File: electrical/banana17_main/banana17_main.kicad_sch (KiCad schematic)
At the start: 25 parts, among them J1 78171-0004, U1 RP2040, U2 NCP1117-3.3_SOT223, U3 W25Q128JVS, Y1 ABMB-272-T3

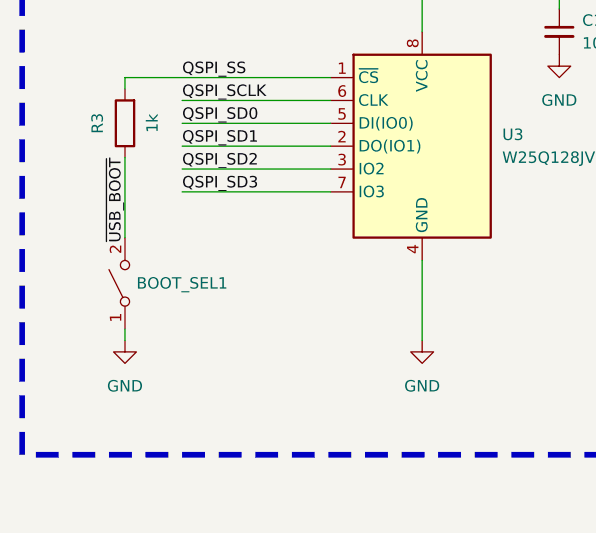
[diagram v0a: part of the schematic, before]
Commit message: Reverted change for SSD1306 library import.
Reverted change for SSD1306 library import.
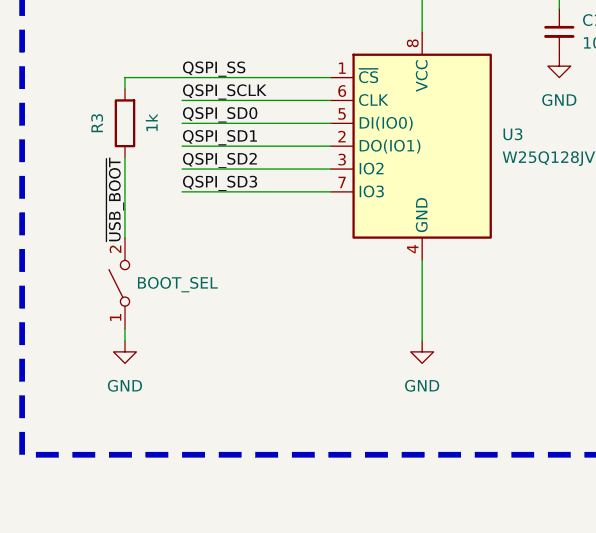
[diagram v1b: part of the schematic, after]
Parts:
- renumbered BOOT_SEL1 to BOOT_SEL
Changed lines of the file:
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@@
 		(on_board yes)
 		(dnp no)
-		(property "Reference" "#PWR019"
+		(property "Reference" "#PWR017"
 			(at 115.57 167.64 0)
 			(effects
@@
 			(project "banana17_main"
 				(path "/fd2b462c-d7c2-4bbf-9a41-8b3fef737a65"
-					(reference "#PWR019")
+					(reference "#PWR017")
 					(unit 1)
 				)
@@
 		(on_board yes)
 		(dnp no)
-		(property "Reference" "#PWR017"
+		(property "Reference" "#PWR019"
 			(at 129.54 160.02 0)
 			(effects
@@
 			(project "banana17_main"
 				(path "/fd2b462c-d7c2-4bbf-9a41-8b3fef737a65"
-					(reference "#PWR017")
+					(reference "#PWR019")
 					(unit 1)
 				)
@@
 		(dnp no)
 		(fields_autoplaced yes)
-		(property "Reference" "#PWR01"
+		(property "Reference" "#PWR03"
 			(at 219.71 39.37 0)
 			(effects
@@
 			(project "banana17_main"
 				(path "/fd2b462c-d7c2-4bbf-9a41-8b3fef737a65"
-					(reference "#PWR01")
+					(reference "#PWR03")
 					(unit 1)
 				)
@@
 		(on_board yes)
 		(dnp no)
-		(property "Reference" "#PWR013"
+		(property "Reference" "#PWR020"
 			(at 137.16 107.95 0)
 			(effects
@@
 			(project "banana17_main"
 				(path "/fd2b462c-d7c2-4bbf-9a41-8b3fef737a65"
-					(reference "#PWR013")
+					(reference "#PWR020")
 					(unit 1)
 				)
@@
 		(on_board yes)
 		(dnp no)
-		(property "Reference" "#PWR07"
+		(property "Reference" "#PWR021"
 			(at 151.13 90.17 0)
 			(effects
@@
 			(project "banana17_main"
 				(path "/fd2b462c-d7c2-4bbf-9a41-8b3fef737a65"
-					(reference "#PWR07")
+					(reference "#PWR021")
 					(unit 1)
 				)
@@
 		(dnp no)
 		(fields_autoplaced yes)
-		(property "Reference" "#PWR010"
+		(property "Reference" "#PWR08"
 			(at 43.18 107.95 0)
 			(effects
@@
 			(project "banana17_main"
 				(path "/fd2b462c-d7c2-4bbf-9a41-8b3fef737a65"
-					(reference "#PWR010")
+					(reference "#PWR08")
 					(unit 1)
 				)
@@
 		(dnp no)
 		(fields_autoplaced yes)
-		(property "Reference" "BOOT_SEL1"
+		(property "Reference" "BOOT_SEL"
 			(at 36.83 168.9099 90)
 			(effects
@@
 			(project "banana17_main"
 				(path "/fd2b462c-d7c2-4bbf-9a41-8b3fef737a65"
-					(reference "BOOT_SEL1")
+					(reference "BOOT_SEL")
 					(unit 1)
 				)
@@
 		(on_board yes)
 		(dnp no)
-		(property "Reference" "#PWR020"
+		(property "Reference" "#PWR016"
 			(at 35.56 181.61 0)
 			(effects
@@
 			(project "banana17_main"
 				(path "/fd2b462c-d7c2-4bbf-9a41-8b3fef737a65"
-					(reference "#PWR020")
+					(reference "#PWR016")
 					(unit 1)
 				)
@@
 		(dnp no)
 		(fields_autoplaced yes)
-		(property "Reference" "#PWR012"
+		(property "Reference" "#PWR010"
 			(at 83.82 107.95 0)
 			(effects
@@
 			(project "banana17_main"
 				(path "/fd2b462c-d7c2-4bbf-9a41-8b3fef737a65"
-					(reference "#PWR012")
+					(reference "#PWR010")
 					(unit 1)
 				)
@@
 		(dnp no)
 		(fields_autoplaced yes)
-		(property "Reference" "#PWR08"
+		(property "Reference" "#PWR011"
 			(at 30.48 93.98 0)
 			(effects
@@
 			(project "banana17_main"
 				(path "/fd2b462c-d7c2-4bbf-9a41-8b3fef737a65"
-					(reference "#PWR08")
+					(reference "#PWR011")
 					(unit 1)
 				)
@@
 		(dnp no)
 		(fields_autoplaced yes)
-		(property "Reference" "#PWR011"
+		(property "Reference" "#PWR09"
 			(at 63.5 107.95 0)
 			(effects
@@
 			(project "banana17_main"
 				(path "/fd2b462c-d7c2-4bbf-9a41-8b3fef737a65"
-					(reference "#PWR011")
+					(reference "#PWR09")
 					(unit 1)
 				)
@@
 		(dnp no)
 		(fields_autoplaced yes)
-		(property "Reference" "#PWR04"
+		(property "Reference" "#PWR06"
 			(at 110.49 40.64 0)
 			(effects
@@
 			(project "banana17_main"
 				(path "/fd2b462c-d7c2-4bbf-9a41-8b3fef737a65"
-					(reference "#PWR04")
+					(reference "#PWR06")
 					(unit 1)
 				)
@@
 		(dnp no)
 		(fields_autoplaced yes)
-		(property "Reference" "#PWR09"
+		(property "Reference" "#PWR012"
 			(at 99.06 93.98 0)
 			(effects
@@
 			(project "banana17_main"
 				(path "/fd2b462c-d7c2-4bbf-9a41-8b3fef737a65"
-					(reference "#PWR09")
+					(reference "#PWR012")
 					(unit 1)
 				)
@@
 		(dnp no)
 		(fields_autoplaced yes)
-		(property "Reference" "#PWR06"
+		(property "Reference" "#PWR07"
 			(at 110.49 55.88 0)
 			(effects
@@
 			(project "banana17_main"
 				(path "/fd2b462c-d7c2-4bbf-9a41-8b3fef737a65"
-					(reference "#PWR06")
+					(reference "#PWR07")
 					(unit 1)
 				)
@@
 		(dnp no)
 		(fields_autoplaced yes)
-		(property "Reference" "#PWR03"
+		(property "Reference" "#PWR04"
 			(at 45.72 40.64 0)
 			(effects
@@
 			(project "banana17_main"
 				(path "/fd2b462c-d7c2-4bbf-9a41-8b3fef737a65"
-					(reference "#PWR03")
+					(reference "#PWR04")
 					(unit 1)
 				)
@@
 		(dnp no)
 		(fields_autoplaced yes)
-		(property "Reference" "#PWR016"
+		(property "Reference" "#PWR014"
 			(at 83.82 149.86 0)
 			(effects
@@
 			(project "banana17_main"
 				(path "/fd2b462c-d7c2-4bbf-9a41-8b3fef737a65"
-					(reference "#PWR016")
+					(reference "#PWR014")
 					(unit 1)
 				)
@@
 		(dnp no)
 		(fields_autoplaced yes)
-		(property "Reference" "#PWR014"
+		(property "Reference" "#PWR015"
 			(at 68.58 137.16 0)
 			(effects
@@
 			(project "banana17_main"
 				(path "/fd2b462c-d7c2-4bbf-9a41-8b3fef737a65"
-					(reference "#PWR014")
+					(reference "#PWR015")
 					(unit 1)
 				)
@@
 		(dnp no)
 		(fields_autoplaced yes)
-		(property "Reference" "#PWR015"
+		(property "Reference" "#PWR01"
 			(at 223.52 142.24 0)
 			(effects
@@
 			(project "banana17_main"
 				(path "/fd2b462c-d7c2-4bbf-9a41-8b3fef737a65"
-					(reference "#PWR015")
+					(reference "#PWR01")
 					(unit 1)
 				)
@@
 		(dnp no)
 		(fields_autoplaced yes)
-		(property "Reference" "#PWR021"
+		(property "Reference" "#PWR013"
 			(at 68.58 181.61 0)
 			(effects
@@
 			(project "banana17_main"
 				(path "/fd2b462c-d7c2-4bbf-9a41-8b3fef737a65"
-					(reference "#PWR021")
-					(unit 1)
-				)
+					(reference "#PWR013")
+					(unit 1)
+				)

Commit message: Uploaded library for SSD1306 128x32.
Uploaded library for SSD1306 128x32. This needs to be tested first prior to usage.
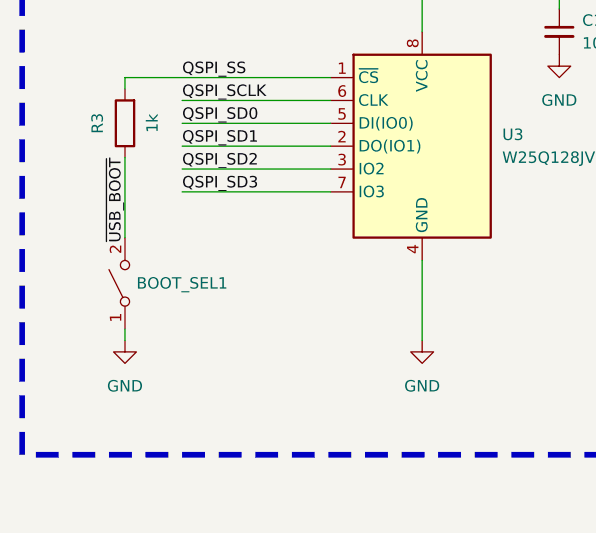
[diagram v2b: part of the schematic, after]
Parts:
- renumbered BOOT_SEL to BOOT_SEL1
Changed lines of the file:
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@@
 		(on_board yes)
 		(dnp no)
-		(property "Reference" "#PWR017"
+		(property "Reference" "#PWR019"
 			(at 115.57 167.64 0)
 			(effects
@@
 			(project "banana17_main"
 				(path "/fd2b462c-d7c2-4bbf-9a41-8b3fef737a65"
-					(reference "#PWR017")
+					(reference "#PWR019")
 					(unit 1)
 				)
@@
 		(on_board yes)
 		(dnp no)
-		(property "Reference" "#PWR019"
+		(property "Reference" "#PWR017"
 			(at 129.54 160.02 0)
 			(effects
@@
 			(project "banana17_main"
 				(path "/fd2b462c-d7c2-4bbf-9a41-8b3fef737a65"
-					(reference "#PWR019")
+					(reference "#PWR017")
 					(unit 1)
 				)
@@
 		(dnp no)
 		(fields_autoplaced yes)
-		(property "Reference" "#PWR03"
+		(property "Reference" "#PWR01"
 			(at 219.71 39.37 0)
 			(effects
@@
 			(project "banana17_main"
 				(path "/fd2b462c-d7c2-4bbf-9a41-8b3fef737a65"
-					(reference "#PWR03")
+					(reference "#PWR01")
 					(unit 1)
 				)
@@
 		(on_board yes)
 		(dnp no)
-		(property "Reference" "#PWR020"
+		(property "Reference" "#PWR013"
 			(at 137.16 107.95 0)
 			(effects
@@
 			(project "banana17_main"
 				(path "/fd2b462c-d7c2-4bbf-9a41-8b3fef737a65"
-					(reference "#PWR020")
+					(reference "#PWR013")
 					(unit 1)
 				)
@@
 		(on_board yes)
 		(dnp no)
-		(property "Reference" "#PWR021"
+		(property "Reference" "#PWR07"
 			(at 151.13 90.17 0)
 			(effects
@@
 			(project "banana17_main"
 				(path "/fd2b462c-d7c2-4bbf-9a41-8b3fef737a65"
-					(reference "#PWR021")
+					(reference "#PWR07")
 					(unit 1)
 				)
@@
 		(dnp no)
 		(fields_autoplaced yes)
-		(property "Reference" "#PWR08"
+		(property "Reference" "#PWR010"
 			(at 43.18 107.95 0)
 			(effects
@@
 			(project "banana17_main"
 				(path "/fd2b462c-d7c2-4bbf-9a41-8b3fef737a65"
-					(reference "#PWR08")
+					(reference "#PWR010")
 					(unit 1)
 				)
@@
 		(dnp no)
 		(fields_autoplaced yes)
-		(property "Reference" "BOOT_SEL"
+		(property "Reference" "BOOT_SEL1"
 			(at 36.83 168.9099 90)
 			(effects
@@
 			(project "banana17_main"
 				(path "/fd2b462c-d7c2-4bbf-9a41-8b3fef737a65"
-					(reference "BOOT_SEL")
+					(reference "BOOT_SEL1")
 					(unit 1)
 				)
@@
 		(on_board yes)
 		(dnp no)
-		(property "Reference" "#PWR016"
+		(property "Reference" "#PWR020"
 			(at 35.56 181.61 0)
 			(effects
@@
 			(project "banana17_main"
 				(path "/fd2b462c-d7c2-4bbf-9a41-8b3fef737a65"
-					(reference "#PWR016")
+					(reference "#PWR020")
 					(unit 1)
 				)
@@
 		(dnp no)
 		(fields_autoplaced yes)
-		(property "Reference" "#PWR010"
+		(property "Reference" "#PWR012"
 			(at 83.82 107.95 0)
 			(effects
@@
 			(project "banana17_main"
 				(path "/fd2b462c-d7c2-4bbf-9a41-8b3fef737a65"
-					(reference "#PWR010")
+					(reference "#PWR012")
 					(unit 1)
 				)
@@
 		(dnp no)
 		(fields_autoplaced yes)
-		(property "Reference" "#PWR011"
+		(property "Reference" "#PWR08"
 			(at 30.48 93.98 0)
 			(effects
@@
 			(project "banana17_main"
 				(path "/fd2b462c-d7c2-4bbf-9a41-8b3fef737a65"
-					(reference "#PWR011")
+					(reference "#PWR08")
 					(unit 1)
 				)
@@
 		(dnp no)
 		(fields_autoplaced yes)
-		(property "Reference" "#PWR09"
+		(property "Reference" "#PWR011"
 			(at 63.5 107.95 0)
 			(effects
@@
 			(project "banana17_main"
 				(path "/fd2b462c-d7c2-4bbf-9a41-8b3fef737a65"
-					(reference "#PWR09")
+					(reference "#PWR011")
 					(unit 1)
 				)
@@
 		(dnp no)
 		(fields_autoplaced yes)
-		(property "Reference" "#PWR06"
+		(property "Reference" "#PWR04"
 			(at 110.49 40.64 0)
 			(effects
@@
 			(project "banana17_main"
 				(path "/fd2b462c-d7c2-4bbf-9a41-8b3fef737a65"
-					(reference "#PWR06")
+					(reference "#PWR04")
 					(unit 1)
 				)
@@
 		(dnp no)
 		(fields_autoplaced yes)
-		(property "Reference" "#PWR012"
+		(property "Reference" "#PWR09"
 			(at 99.06 93.98 0)
 			(effects
@@
 			(project "banana17_main"
 				(path "/fd2b462c-d7c2-4bbf-9a41-8b3fef737a65"
-					(reference "#PWR012")
+					(reference "#PWR09")
 					(unit 1)
 				)
@@
 		(dnp no)
 		(fields_autoplaced yes)
-		(property "Reference" "#PWR07"
+		(property "Reference" "#PWR06"
 			(at 110.49 55.88 0)
 			(effects
@@
 			(project "banana17_main"
 				(path "/fd2b462c-d7c2-4bbf-9a41-8b3fef737a65"
-					(reference "#PWR07")
+					(reference "#PWR06")
 					(unit 1)
 				)
@@
 		(dnp no)
 		(fields_autoplaced yes)
-		(property "Reference" "#PWR04"
+		(property "Reference" "#PWR03"
 			(at 45.72 40.64 0)
 			(effects
@@
 			(project "banana17_main"
 				(path "/fd2b462c-d7c2-4bbf-9a41-8b3fef737a65"
-					(reference "#PWR04")
+					(reference "#PWR03")
 					(unit 1)
 				)
@@
 		(dnp no)
 		(fields_autoplaced yes)
-		(property "Reference" "#PWR014"
+		(property "Reference" "#PWR016"
 			(at 83.82 149.86 0)
 			(effects
@@
 			(project "banana17_main"
 				(path "/fd2b462c-d7c2-4bbf-9a41-8b3fef737a65"
-					(reference "#PWR014")
+					(reference "#PWR016")
 					(unit 1)
 				)
@@
 		(dnp no)
 		(fields_autoplaced yes)
-		(property "Reference" "#PWR015"
+		(property "Reference" "#PWR014"
 			(at 68.58 137.16 0)
 			(effects
@@
 			(project "banana17_main"
 				(path "/fd2b462c-d7c2-4bbf-9a41-8b3fef737a65"
-					(reference "#PWR015")
+					(reference "#PWR014")
 					(unit 1)
 				)
@@
 		(dnp no)
 		(fields_autoplaced yes)
-		(property "Reference" "#PWR01"
+		(property "Reference" "#PWR015"
 			(at 223.52 142.24 0)
 			(effects
@@
 			(project "banana17_main"
 				(path "/fd2b462c-d7c2-4bbf-9a41-8b3fef737a65"
-					(reference "#PWR01")
+					(reference "#PWR015")
 					(unit 1)
 				)
@@
 		(dnp no)
 		(fields_autoplaced yes)
-		(property "Reference" "#PWR013"
+		(property "Reference" "#PWR021"
 			(at 68.58 181.61 0)
 			(effects
@@
 			(project "banana17_main"
 				(path "/fd2b462c-d7c2-4bbf-9a41-8b3fef737a65"
-					(reference "#PWR013")
-					(unit 1)
-				)
+					(reference "#PWR021")
+					(unit 1)
+				)
